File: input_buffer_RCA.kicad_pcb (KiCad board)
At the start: 2 copper layers, 55 x 47.5 mm, 35 parts, among them J1 INPUT, J2 CH1OUT, J3 CH2OUT, J4 POWER, U1 LM4562, U2 LM4562, U3 LM4562

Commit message: minor changes
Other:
- board text added: "Bilous Sound"
- board text added: "May 2023"
- board text added: "Rev1.0"
- board text added: "Switchcraft PJRAS2X1S01X"
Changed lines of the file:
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@@
   (general
     (thickness 1.6)
-    (drawings 19)
+    (drawings 23)
     (tracks 375)
     (zones 0)
@@
   )
   (setup
-    (last_trace_width 0.5)
+    (last_trace_width 0.3)
     (user_trace_width 0.5)
     (user_trace_width 1)
@@
       (effects (font (size 1 1) (thickness 0.15)))
     )
-    (fp_text user %R (at 0.3 0) (layer F.Fab)
-      (effects (font (size 1 1) (thickness 0.15)))
-    )
     (fp_circle (center 0 0) (end 3.2 0) (layer Cmts.User) (width 0.15))
     (fp_circle (center 0 0) (end 3.45 0) (layer F.CrtYd) (width 0.05))
+    (fp_text user %R (at 0.3 0) (layer F.Fab)
+      (effects (font (size 1 1) (thickness 0.15)))
+    )
     (pad 1 thru_hole circle (at 1.697056 -1.697056) (size 0.8 0.8) (drill 0.5) (layers *.Cu *.Mask))
     (pad 1 thru_hole circle (at 0 -2.4) (size 0.8 0.8) (drill 0.5) (layers *.Cu *.Mask))
@@
       (effects (font (size 1 1) (thickness 0.15)))
     )
-    (fp_text user %R (at 0.3 0) (layer F.Fab)
-      (effects (font (size 1 1) (thickness 0.15)))
-    )
     (fp_circle (center 0 0) (end 3.2 0) (layer Cmts.User) (width 0.15))
     (fp_circle (center 0 0) (end 3.45 0) (layer F.CrtYd) (width 0.05))
+    (fp_text user %R (at 0.3 0) (layer F.Fab)
+      (effects (font (size 1 1) (thickness 0.15)))
+    )
     (pad 1 thru_hole circle (at 1.697056 -1.697056) (size 0.8 0.8) (drill 0.5) (layers *.Cu *.Mask))
     (pad 1 thru_hole circle (at 0 -2.4) (size 0.8 0.8) (drill 0.5) (layers *.Cu *.Mask))
@@
       (effects (font (size 1 1) (thickness 0.15)))
     )
-    (fp_text user %R (at 0.3 0) (layer F.Fab)
-      (effects (font (size 1 1) (thickness 0.15)))
-    )
     (fp_circle (center 0 0) (end 3.2 0) (layer Cmts.User) (width 0.15))
     (fp_circle (center 0 0) (end 3.45 0) (layer F.CrtYd) (width 0.05))
+    (fp_text user %R (at 0.3 0) (layer F.Fab)
+      (effects (font (size 1 1) (thickness 0.15)))
+    )
     (pad 1 thru_hole circle (at 1.697056 -1.697056) (size 0.8 0.8) (drill 0.5) (layers *.Cu *.Mask))
     (pad 1 thru_hole circle (at 0 -2.4) (size 0.8 0.8) (drill 0.5) (layers *.Cu *.Mask))
@@
       (effects (font (size 1 1) (thickness 0.15)))
     )
-    (fp_text user %R (at 0.3 0) (layer F.Fab)
-      (effects (font (size 1 1) (thickness 0.15)))
-    )
     (fp_circle (center 0 0) (end 3.2 0) (layer Cmts.User) (width 0.15))
     (fp_circle (center 0 0) (end 3.45 0) (layer F.CrtYd) (width 0.05))
+    (fp_text user %R (at 0.3 0) (layer F.Fab)
+      (effects (font (size 1 1) (thickness 0.15)))
+    )
     (pad 1 thru_hole circle (at 1.697056 -1.697056) (size 0.8 0.8) (drill 0.5) (layers *.Cu *.Mask))
     (pad 1 thru_hole circle (at 0 -2.4) (size 0.8 0.8) (drill 0.5) (layers *.Cu *.Mask))
@@
     )
     (fp_text value SMF6.0 (at 0 2.1) (layer F.Fab)
-      (effects (font (size 1 1) (thickness 0.15)))
-    )
-    (fp_text user %R (at 0 -2) (layer F.Fab)
       (effects (font (size 1 1) (thickness 0.15)))
     )
@@
     (fp_line (start -2.25 1) (end 1.65 1) (layer F.SilkS) (width 0.12))
     (fp_line (start -2.25 -1) (end 1.65 -1) (layer F.SilkS) (width 0.12))
+    (fp_text user %R (at 0 -2) (layer F.Fab)
+      (effects (font (size 1 1) (thickness 0.15)))
+    )
     (pad 2 smd rect (at 1.65 0) (size 0.9 1.2) (layers F.Cu F.Paste F.Mask)
       (net 17 "Net-(D2-Pad2)"))
@@
     )
     (fp_text value SMF6.0 (at 0 2.1) (layer F.Fab)
-      (effects (font (size 1 1) (thickness 0.15)))
-    )
-    (fp_text user %R (at 0 -2) (layer F.Fab)
       (effects (font (size 1 1) (thickness 0.15)))
     )
@@
     (fp_line (start -2.25 1) (end 1.65 1) (layer F.SilkS) (width 0.12))
     (fp_line (start -2.25 -1) (end 1.65 -1) (layer F.SilkS) (width 0.12))
+    (fp_text user %R (at 0 -2) (layer F.Fab)
+      (effects (font (size 1 1) (thickness 0.15)))
+    )
     (pad 2 smd rect (at 1.65 0 180) (size 0.9 1.2) (layers F.Cu F.Paste F.Mask)
       (net 16 "Net-(D1-Pad2)"))
@@
       (rotate (xyz 0 0 0))
     )
+  )
+  (gr_text "Switchcraft PJRAS2X1S01X" (at 141.5 138.5 90) (layer F.SilkS)
+    (effects (font (size 1 1) (thickness 0.15)))
+  )
+  (gr_text Rev1.0 (at 142.5 135.75) (layer B.SilkS)
+    (effects (font (size 1 1) (thickness 0.15)) (justify mirror))
+  )
+  (gr_text "May 2023" (at 143 133) (layer B.SilkS)
+    (effects (font (size 1 1) (thickness 0.15)) (justify mirror))
+  )
+  (gr_text "Bilous Sound" (at 99.75 132 90) (layer F.SilkS)
+    (effects (font (size 1 1) (thickness 0.15) italic))
   )
   (gr_text CH2 (at 137.75 136.75) (layer F.SilkS)
@@
   (segment (start 126.75 124.5) (end 124.75 124.5) (width 0.5) (layer F.Cu) (net 5))
   (segment (start 127.5 123.75) (end 126.75 124.5) (width 0.5) (layer F.Cu) (net 5))
-  (segment (start 108.5 106.25) (end 108.5 108.25) (width 0.3) (layer F.Cu) (net 18))
-  (segment (start 108.5 108.25) (end 105.5 111.25) (width 0.3) (layer F.Cu) (net 18))
-  (segment (start 105.5 111.25) (end 102.25 111.25) (width 0.3) (layer F.Cu) (net 18))
-  (segment (start 101.5 112) (end 101.5 113.7625) (width 0.3) (layer F.Cu) (net 18))
-  (segment (start 102.25 111.25) (end 101.5 112) (width 0.3) (layer F.Cu) (net 18))
-  (segment (start 115.75 113.7625) (end 115.75 112.5) (width 0.3) (layer F.Cu) (net 19))
-  (segment (start 112 108.25) (end 115.75 112) (width 0.3) (layer F.Cu) (net 19))
-  (segment (start 112 108.25) (end 112 106.25) (width 0.3) (layer F.Cu) (net 19))
-  (segment (start 115.75 112) (end 115.75 112.5) (width 0.3) (layer F.Cu) (net 19))
-  (segment (start 138 106.25) (end 138 108.25) (width 0.3) (layer F.Cu) (net 20))
-  (segment (start 134 112.25) (end 134 113.7625) (width 0.3) (layer F.Cu) (net 20))
-  (segment (start 138 108.25) (end 134 112.25) (width 0.3) (layer F.Cu) (net 20))
   (segment (start 119.1025 117.615) (end 119 117.5125) (width 0.3) (layer F.Cu) (net 6))
   (segment (start 122.525 117.615) (end 119.1025 117.615) (width 0.3) (layer F.Cu) (net 6))
@@
   (segment (start 131.65 131.1625) (end 131.4875 131) (width 0.3) (layer F.Cu) (net 17))
   (segment (start 131.65 133.75) (end 131.65 131.1625) (width 0.3) (layer F.Cu) (net 17))
+  (segment (start 108.5 106.25) (end 108.5 108.25) (width 0.3) (layer F.Cu) (net 18))
+  (segment (start 108.5 108.25) (end 105.5 111.25) (width 0.3) (layer F.Cu) (net 18))
+  (segment (start 105.5 111.25) (end 102.25 111.25) (width 0.3) (layer F.Cu) (net 18))
+  (segment (start 101.5 112) (end 101.5 113.7625) (width 0.3) (layer F.Cu) (net 18))
+  (segment (start 102.25 111.25) (end 101.5 112) (width 0.3) (layer F.Cu) (net 18))
+  (segment (start 115.75 113.7625) (end 115.75 112.5) (width 0.3) (layer F.Cu) (net 19))
+  (segment (start 112 108.25) (end 115.75 112) (width 0.3) (layer F.Cu) (net 19))
+  (segment (start 112 108.25) (end 112 106.25) (width 0.3) (layer F.Cu) (net 19))
+  (segment (start 115.75 112) (end 115.75 112.5) (width 0.3) (layer F.Cu) (net 19))
+  (segment (start 138 106.25) (end 138 108.25) (width 0.3) (layer F.Cu) (net 20))
+  (segment (start 134 112.25) (end 134 113.7625) (width 0.3) (layer F.Cu) (net 20))
+  (segment (start 138 108.25) (end 134 112.25) (width 0.3) (layer F.Cu) (net 20))
   (segment (start 148.25 113.7625) (end 148.25 112.25) (width 0.3) (layer F.Cu) (net 21))
   (segment (start 148.25 112.25) (end 147.25 111.25) (width 0.3) (layer F.Cu) (net 21))

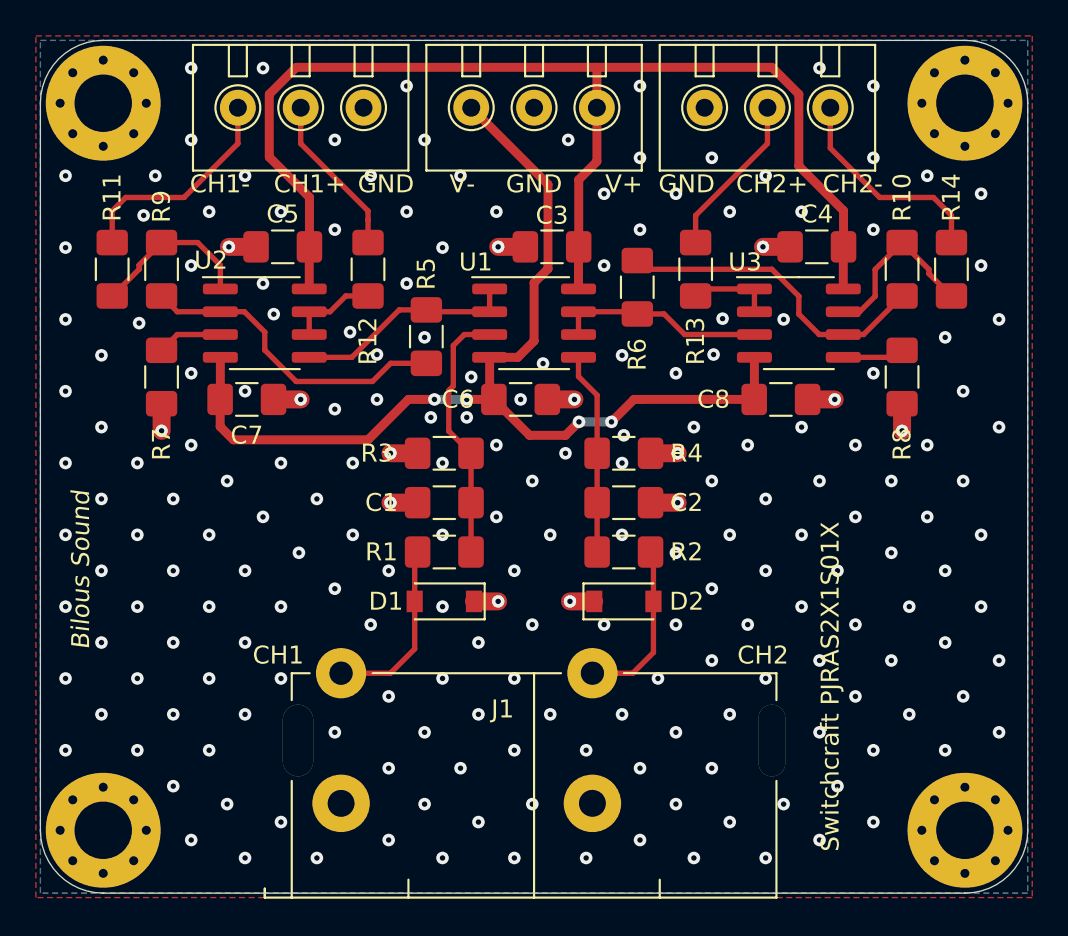
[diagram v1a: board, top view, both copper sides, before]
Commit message: rearranged components to reduce board size
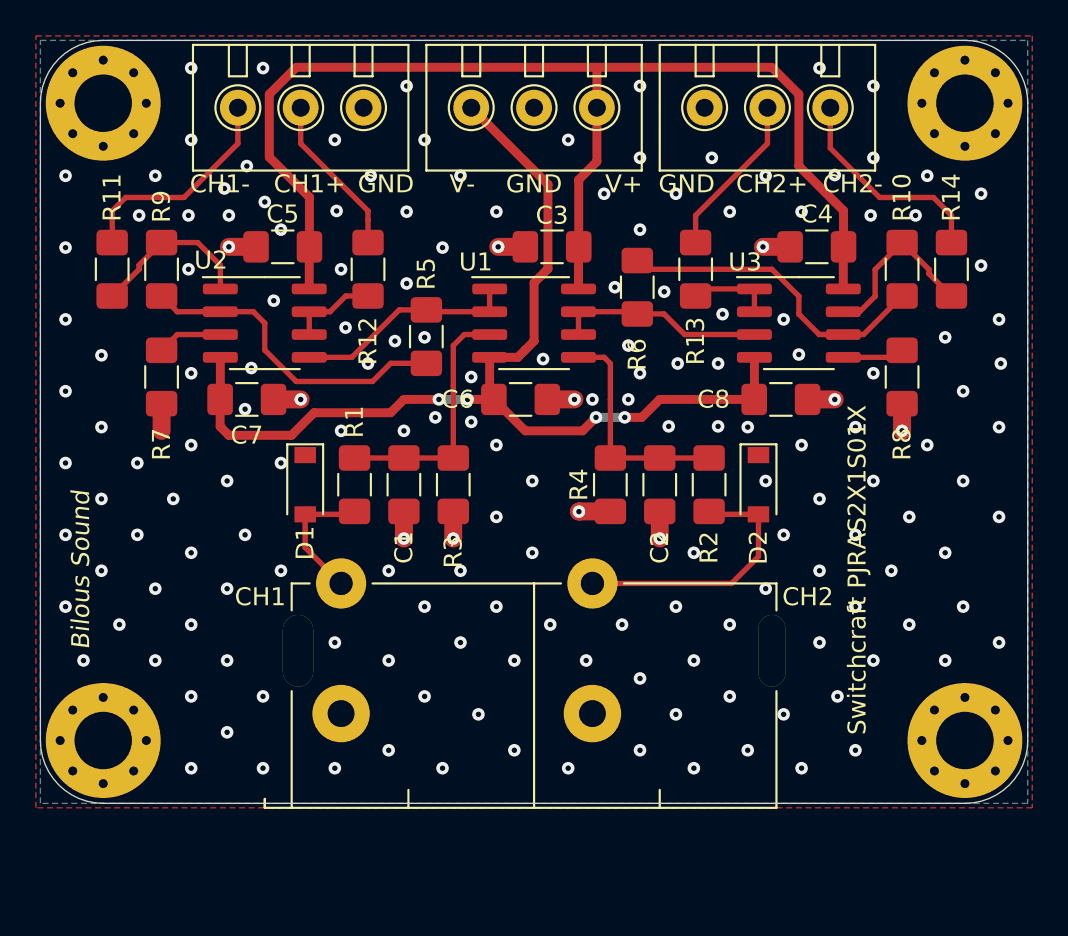
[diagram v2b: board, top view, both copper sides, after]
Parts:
- moved D1 10.1 mm to (112.2, 127.2), turned to 270 degrees
- moved D2 9.92 mm to (137.5, 127.2), turned to 270 degrees
- moved R1 6.25 mm to (115.0, 127.2), turned to 270 degrees
- moved R2 6.05 mm to (134.8, 127.2), turned to 270 degrees
- moved H2 5.00 mm to (101.0, 141.5)
- moved H4 5.00 mm to (149.0, 141.5)
- moved J1 5.00 mm to (111.5, 145.2)
- moved C1 2.46 mm to (117.8, 127.2), turned to 90 degrees
- moved C2 2.24 mm to (132.0, 127.2), turned to 90 degrees
- moved R4 1.90 mm to (129.2, 127.2), turned to 90 degrees
- moved R3 1.82 mm to (120.5, 127.2), turned to 90 degrees
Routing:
- net Net-(D2-Pad2): track 9.54 -> 15.0 mm
- net Net-(D1-Pad2): track 10.1 -> 7.50 mm
- net GND: track 20.8 -> 18.4 mm, vias 214 -> 177
- net Net-(C2-Pad2): track 11.3 -> 12.7 mm
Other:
- board size 55 x 47.5 mm -> 55 x 42.5 mm

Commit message: rev2
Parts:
- D1, D2: footprint Diode_SMD:D_SOD-123 -> Diode_SMD:D_SOD-123F
- J4: footprint local_footprint_lib:TerminalBlock_ Amphenol_01_03_P3.50mm -> local_footprint_lib:TerminalBlock_ Amphenol_01_02_P3.50mm
- R11, R12, R13, R14: value 22R -> 100R
- moved H2 2.75 mm to (101.0, 138.8)
- moved H4 2.75 mm to (149.0, 138.8)
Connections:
- J4 pad 2: GND -> VEE
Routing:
- net VEE: track 58.8 -> 58.1 mm
- net GND: vias 177 -> 172
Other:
- board text added: "Rev2.0"
- board text removed: "Rev1.0"
